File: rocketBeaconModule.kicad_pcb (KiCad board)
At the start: 2 copper layers, 80.5 x 49.3 mm, 72 parts, among them J1 TYPE-C-31-M-12, J2 Jumper Select, J3 Main Bus, P1 AntMount, U1 STM32F401CCU6, U2 AMS1117-3.3, U3 CC1200, X1 40mhz, Y1 16MHz

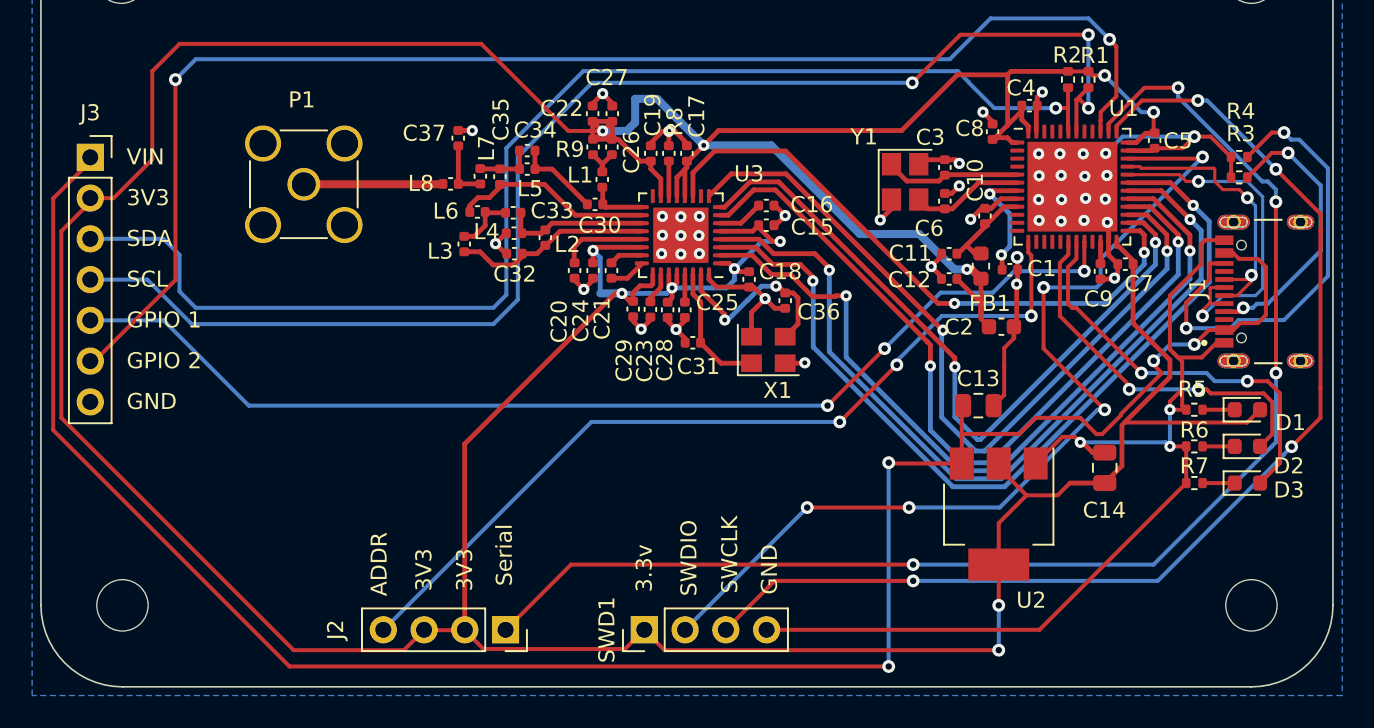
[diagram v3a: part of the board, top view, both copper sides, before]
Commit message: updated silk screen\nincreased spacing between leds\nchanged version number to 2.0
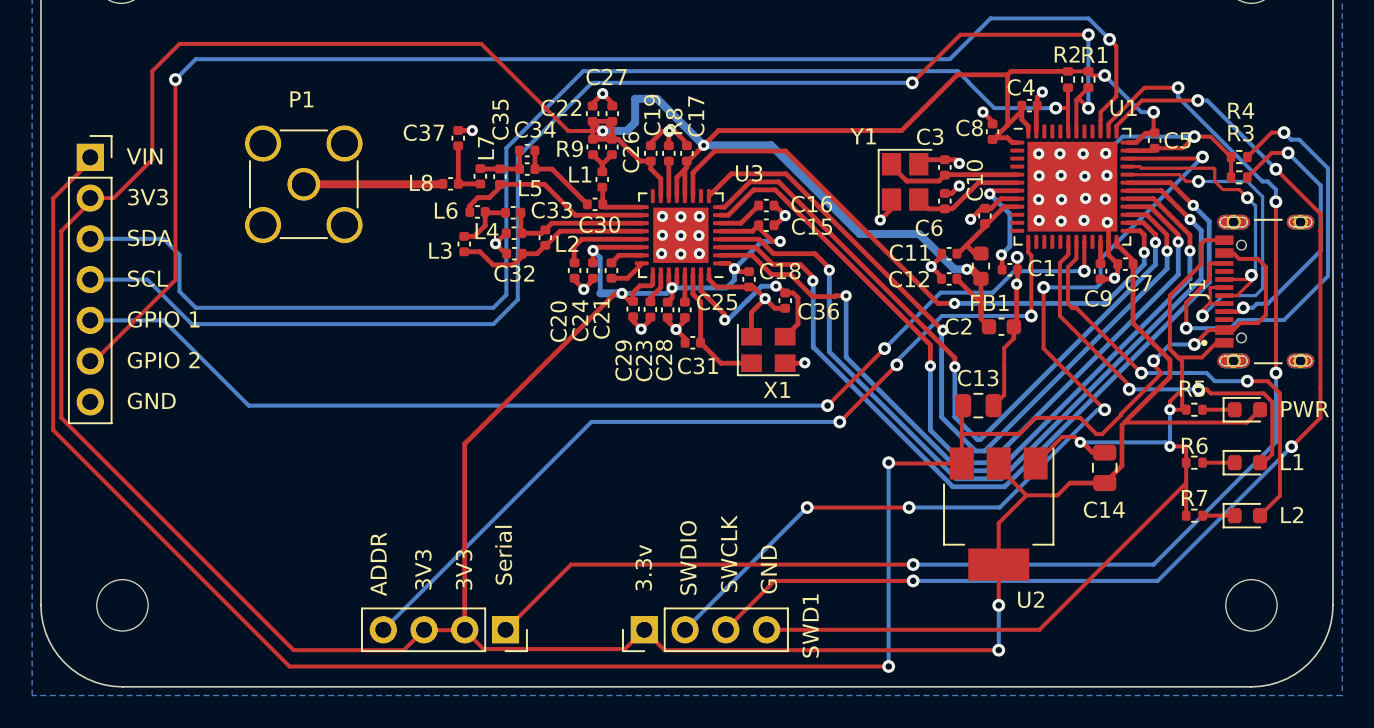
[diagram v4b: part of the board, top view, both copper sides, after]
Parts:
- J2: value Jumper Select -> MODE
- moved D3 2.03 mm to (225.0, 104.9)
- moved R7 2.03 mm to (221.7, 104.9)
- moved D2 1.02 mm to (225.0, 101.6)
- moved R6 1.02 mm to (221.7, 101.6)
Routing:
- net GND: track 136.8 -> 138.8 mm
- net /LED2: track 25.7 -> 27.7 mm
- net /LED1: track 23.5 -> 24.7 mm
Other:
- board text added: "L1"
- board text added: "L2"
- board text added: "PWR"
- board text added: "v2.0"
- board text removed: "v1.0"
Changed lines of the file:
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@@
   )
   (footprint "Resistor_SMD:R_0402_1005Metric" (layer "F.Cu")
-    (at 221.742 100.584 180)
+    (at 221.742 101.6 180)
     (descr "Resistor SMD 0402 (1005 Metric), square (rectangular) end terminal, IPC_7351 nominal, (Body size source: IPC-SM-782 page 72, https://www.pcb-3d.com/wordpress/wp-content/uploads/ipc-sm-782a_amendment_1_and_2.pdf), generated with kicad-footprint-generator")
     (tags "resistor")
@@
     (property "Sheetname" "")
     (attr smd)
-    (fp_text reference "D1" (at 2.688 0.808 180) (layer "F.SilkS")
+    (fp_text reference "D1" (at 2.688 0.808 180) (layer "F.SilkS") hide
       (effects (font (size 1 1) (thickness 0.15)))
     )
@@
   )
   (footprint "Resistor_SMD:R_0402_1005Metric" (layer "F.Cu")
-    (at 221.742 102.87 180)
+    (at 221.742 104.902 180)
     (descr "Resistor SMD 0402 (1005 Metric), square (rectangular) end terminal, IPC_7351 nominal, (Body size source: IPC-SM-782 page 72, https://www.pcb-3d.com/wordpress/wp-content/uploads/ipc-sm-782a_amendment_1_and_2.pdf), generated with kicad-footprint-generator")
     (tags "resistor")
@@
   )
   (footprint "LED_SMD:LED_0603_1608Metric" (layer "F.Cu")
-    (at 225.044 100.584)
+    (at 225.044 101.6)
     (descr "LED SMD 0603 (1608 Metric), square (rectangular) end terminal, IPC_7351 nominal, (Body size source: http://www.tortai-tech.com/upload/download/2011102023233369053.pdf), generated with kicad-footprint-generator")
     (tags "LED")
@@
     (property "Sheetname" "")
     (attr smd)
-    (fp_text reference "D2" (at 2.588 1.222) (layer "F.SilkS")
+    (fp_text reference "D2" (at 2.588 1.222) (layer "F.SilkS") hide
       (effects (font (size 1 1) (thickness 0.15)))
     )
-    (fp_text value "LED" (at 0 1.43) (layer "F.Fab")
+    (fp_text value "LED" (at 0 1.43) (layer "F.Fab") hide
       (effects (font (size 1 1) (thickness 0.15)))
     )
@@
     (property "Sheetname" "")
     (attr through_hole)
-    (fp_text reference "J2" (at 0 10.584 90) (layer "F.SilkS")
+    (fp_text reference "J2" (at 0 10.584 90) (layer "F.SilkS") hide
       (effects (font (size 1 1) (thickness 0.15)))
     )
-    (fp_text value "Jumper Select" (at 0 10.39 90) (layer "F.Fab")
+    (fp_text value "MODE" (at 0 10.39 90) (layer "F.Fab")
       (effects (font (size 1 1) (thickness 0.15)))
     )
@@
   )
   (footprint "LED_SMD:LED_0603_1608Metric" (layer "F.Cu")
-    (at 225.044 102.87)
+    (at 225.044 104.902)
     (descr "LED SMD 0603 (1608 Metric), square (rectangular) end terminal, IPC_7351 nominal, (Body size source: http://www.tortai-tech.com/upload/download/2011102023233369053.pdf), generated with kicad-footprint-generator")
     (tags "LED")
@@
     (property "Sheetname" "")
     (attr smd)
-    (fp_text reference "D3" (at 2.588 0.436) (layer "F.SilkS")
+    (fp_text reference "D3" (at 2.588 0.436) (layer "F.SilkS") hide
       (effects (font (size 1 1) (thickness 0.15)))
     )
-    (fp_text value "LED" (at 0 1.43) (layer "F.Fab")
+    (fp_text value "LED" (at 0 1.43) (layer "F.Fab") hide
       (effects (font (size 1 1) (thickness 0.15)))
     )
@@
     (property "Sheetname" "")
     (attr through_hole)
-    (fp_text reference "SWD1" (at 0 -2.33 90) (layer "F.SilkS")
+    (fp_text reference "SWD1" (at 0.254 10.404 90) (layer "F.SilkS")
       (effects (font (size 1 1) (thickness 0.15)))
     )
@@
     (property "Sheetname" "")
     (attr through_hole)
-    (fp_text reference "J3" (at 0 -2.77) (layer "F.SilkS")
+    (fp_text reference "J3" (at 0 -2.77) (layer "F.SilkS") hide
       (effects (font (size 1 1) (thickness 0.15)))
     )
@@
     (effects (font (size 2 2) (thickness 0.3)) (justify mirror))
   )
-  (gr_text "v1.0" (at 218.44 105.918) (layer "B.SilkS")
+  (gr_text "v2.0" (at 218.44 105.918) (layer "B.SilkS")
     (effects (font (size 1 1) (thickness 0.15)) (justify mirror))
   )
@@
     (effects (font (size 1 1) (thickness 0.15)) (justify right))
   )
+  (gr_text "L2" (at 227.838 104.902) (layer "F.SilkS")
+    (effects (font (size 1 1) (thickness 0.15)))
+  )
+  (gr_text "PWR" (at 228.6 98.298) (layer "F.SilkS")
+    (effects (font (size 1 1) (thickness 0.15)))
+  )
   (gr_text "GPIO 1" (at 155.194 92.71) (layer "F.SilkS")
     (effects (font (size 1 1) (thickness 0.15)) (justify left))
@@
     (effects (font (size 1 1) (thickness 0.15)) (justify left))
   )
+  (gr_text "L1" (at 227.838 101.6) (layer "F.SilkS")
+    (effects (font (size 1 1) (thickness 0.15)))
+  )
   (segment (start 209.76125 89.575) (end 209.76125 88.695) (width 0.3) (layer "F.Cu") (net 1))
   (segment (start 209.19075 84.65) (end 208.99125 84.8495) (width 0.3) (layer "F.Cu") (net 1))
@@
   (segment (start 216.154 100.97) (end 215.404 100.97) (width 0.3) (layer "F.Cu") (net 2))
   (segment (start 190.11625 81.845) (end 190.11625 81.7) (width 0.3) (layer "F.Cu") (net 2))
+  (segment (start 221.232 104.902) (end 221.232 102.87) (width 0.25) (layer "F.Cu") (net 2))
   (segment (start 195.61625 85.575) (end 196.24125 86.2) (width 0.3) (layer "F.Cu") (net 2))
   (segment (start 195.64125 86.8) (end 196.24125 86.2) (width 0.3) (layer "F.Cu") (net 2))
@@
   (segment (start 174.91125 84.225) (end 174.88625 84.25) (width 0.5) (layer "F.Cu") (net 32))
   (segment (start 174.88625 84.25) (end 166.24125 84.25) (width 0.5) (layer "F.Cu") (net 32))
-  (segment (start 222.252 100.584) (end 224.2565 100.584) (width 0.25) (layer "F.Cu") (net 35))
-  (segment (start 225.8315 100.584) (end 226.594 99.8215) (width 0.25) (layer "F.Cu") (net 36))
-  (segment (start 226.594 99.8215) (end 226.594 97.816521) (width 0.25) (layer "F.Cu") (net 36))
+  (segment (start 222.252 101.6) (end 224.2565 101.6) (width 0.25) (layer "F.Cu") (net 35))
+  (segment (start 226.594 101.066) (end 226.594 97.816521) (width 0.25) (layer "F.Cu") (net 36))
+  (segment (start 222.758 97.282) (end 222.504 97.028) (width 0.25) (layer "F.Cu") (net 36))
+  (segment (start 226.059478 97.282) (end 222.758 97.282) (width 0.25) (layer "F.Cu") (net 36))
   (segment (start 222.504 97.028) (end 221.996 97.028) (width 0.25) (layer "F.Cu") (net 36))
   (segment (start 213.89125 88.62275) (end 213.89125 87.8375) (width 0.25) (layer "F.Cu") (net 36))
-  (segment (start 226.594 97.816521) (end 226.059478 97.282) (width 0.25) (layer "F.Cu") (net 36))
   (segment (start 213.36 92.456) (end 213.36 89.154) (width 0.25) (layer "F.Cu") (net 36))
   (segment (start 213.36 89.154) (end 213.89125 88.62275) (width 0.25) (layer "F.Cu") (net 36))
-  (segment (start 222.758 97.282) (end 222.504 97.028) (width 0.25) (layer "F.Cu") (net 36))
+  (segment (start 225.8315 101.6) (end 226.06 101.6) (width 0.25) (layer "F.Cu") (net 36))
+  (segment (start 226.594 97.816521) (end 226.059478 97.282) (width 0.25) (layer "F.Cu") (net 36))
+  (segment (start 226.06 101.6) (end 226.594 101.066) (width 0.25) (layer "F.Cu") (net 36))
   (segment (start 217.678 96.774) (end 213.36 92.456) (width 0.25) (layer "F.Cu") (net 36))
-  (segment (start 226.059478 97.282) (end 222.758 97.282) (width 0.25) (layer "F.Cu") (net 36))
   (segment (start 217.678 97.028) (end 217.678 96.774) (width 0.25) (layer "F.Cu") (net 36))
   (via (at 217.678 97.028) (size 0.8) (drill 0.4) (layers "F.Cu" "B.Cu") (net 36))
@@
   (segment (start 229.616758 88.391242) (end 229.616758 84.328758) (width 0.25) (layer "B.Cu") (net 43))
   (segment (start 229.616758 84.328758) (end 227.584 82.296) (width 0.25) (layer "B.Cu") (net 43))
-  (segment (start 222.252 102.87) (end 224.2565 102.87) (width 0.25) (layer "F.Cu") (net 44))
-  (segment (start 227.076 97.282) (end 227.076 101.6255) (width 0.25) (layer "F.Cu") (net 45))
+  (segment (start 224.2565 104.902) (end 222.252 104.902) (width 0.25) (layer "F.Cu") (net 44))
+  (segment (start 227.076 103.6575) (end 225.8315 104.902) (width 0.25) (layer "F.Cu") (net 45))
   (segment (start 214.39125 91.96325) (end 218.44 96.012) (width 0.25) (layer "F.Cu") (net 45))
   (segment (start 213.868 91.694) (end 214.13725 91.96325) (width 0.25) (layer "F.Cu") (net 45))
   (segment (start 214.39125 88.88475) (end 213.868 89.408) (width 0.25) (layer "F.Cu") (net 45))
-  (segment (start 227.076 101.6255) (end 225.8315 102.87) (width 0.25) (layer "F.Cu") (net 45))
-  (segment (start 226.568 96.774) (end 227.076 97.282) (width 0.25) (layer "F.Cu") (net 45))
-  (segment (start 226.568 96.774) (end 226.314 96.52) (width 0.25) (layer "F.Cu") (net 45))
-  (segment (start 226.314 96.52) (end 225.044 96.52) (width 0.25) (layer "F.Cu") (net 45))
+  (segment (start 225.044 96.52) (end 226.314 96.52) (width 0.25) (layer "F.Cu") (net 45))
+  (segment (start 226.314 96.52) (end 227.076 97.282) (width 0.25) (layer "F.Cu") (net 45))
   (segment (start 214.13725 91.96325) (end 214.39125 91.96325) (width 0.25) (layer "F.Cu") (net 45))
   (segment (start 213.868 89.408) (end 213.868 91.694) (width 0.25) (layer "F.Cu") (net 45))
   (segment (start 214.39125 87.8375) (end 214.39125 88.88475) (width 0.25) (layer "F.Cu") (net 45))
+  (segment (start 227.076 97.282) (end 227.076 103.6575) (width 0.25) (layer "F.Cu") (net 45))
   (via (at 218.44 96.012) (size 0.8) (drill 0.4) (layers "F.Cu" "B.Cu") (net 45))
   (via (at 225.044 96.52) (size 0.8) (drill 0.4) (layers "F.Cu" "B.Cu") (net 45))

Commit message: Set Version 1.1
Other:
- board text added: "v1.1"
- board text removed: "v2.0"
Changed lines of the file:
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@@
     (effects (font (size 2 2) (thickness 0.3)) (justify mirror))
   )
-  (gr_text "v2.0" (at 218.44 105.918) (layer "B.SilkS")
+  (gr_text "v1.1" (at 218.44 105.918) (layer "B.SilkS")
     (effects (font (size 1 1) (thickness 0.15)) (justify mirror))
   )

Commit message: V3 changes
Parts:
- removed C14: 22u, Capacitor_SMD:C_0805_2012Metric
- removed J2: MODE, Connector_PinSocket_2.54mm:PinSocket_1x04_P2.54mm_Vertical
- removed J3: Main Bus, Connector_PinSocket_2.54mm:PinSocket_1x07_P2.54mm_Vertical
- removed R2: 1.5k, Resistor_SMD:R_0402_1005Metric
- added D4: TXT, LED_SMD:LED_0402_1005Metric, F.Cu at (93.7, 117.9)
- added D5: RXT, LED_SMD:LED_0402_1005Metric, F.Cu at (93.7, 118.9)
- added EX1: EXT1, Connector_FFC-FPC:Molex_200528-0080_1x08-1MP_P1.00mm_Horizontal, F.Cu at (72.0, 111.2)
- added R10: 1k, Resistor_SMD:R_0402_1005Metric, F.Cu at (93.7, 116.8)
- added R11: 1k, Resistor_SMD:R_0402_1005Metric, F.Cu at (93.7, 119.9)
- added R12: 5.11k, Resistor_SMD:R_0402_1005Metric, F.Cu at (84.2, 120.1)
- C1: value 100n -> 4.7uF; footprint Capacitor_SMD:C_0402_1005Metric -> Capacitor_SMD:C_0603_1608Metric
- C10: value 10n -> 10nF
- C11, C12: value 1u -> 1uF
- C13: value 22u -> 100nF; footprint Capacitor_SMD:C_0805_2012Metric -> Capacitor_SMD:C_0402_1005Metric
- C2: value 10u -> 10uF
- C3, C6: value 10p -> 10pF
- C4, C5, C7, C8: value 100n -> 100nF
- C9: value 2.2u -> 2.2uF
- D1: value LED -> PWR_LED; footprint LED_SMD:LED_0603_1608Metric -> LED_SMD:LED_0402_1005Metric
- D2, D3: footprint LED_SMD:LED_0603_1608Metric -> LED_SMD:LED_0402_1005Metric
- H1, H2, H3, H4: footprint MountingHole:MountingHole_3.2mm_M3 -> MountingHole:MountingHole_2.2mm_M2
- R1: value 1.5k -> 5.11k
- R9: value 18 -> 18k
- SWD1: footprint Connector_PinHeader_2.54mm:PinHeader_1x04_P2.54mm_Vertical -> Connector_PinSocket_1.27mm:PinSocket_1x05_P1.27mm_Vertical
- U2: value AMS1117-3.3 -> CP2102N-Axx-xQFN20; footprint Package_TO_SOT_SMD:SOT-223-3_TabPin2 -> CP2102:WFQFN-20
- X1: value 40mhz -> 40MHz
- moved H3 181.8 mm to (57.5, 141.2)
- moved D2 177.6 mm to (50.3, 133.3)
- moved D3 177.2 mm to (50.3, 134.4)
- moved R6 174.2 mm to (50.3, 132.3), turned to 0 degrees
- moved R7 174.1 mm to (50.3, 135.4), turned to 0 degrees
- moved C5 163.3 mm to (64.8, 134.5), turned to 0 degrees
- moved C7 160.6 mm to (63.3, 134.1), turned to 90 degrees
- moved FB1 159.0 mm to (59.6, 145.0)
- moved C9 156.8 mm to (68.9, 144.4)
- moved C6 156.8 mm to (58.5, 138.2), turned to 180 degrees
- moved U1 156.4 mm to (67.6, 139.3)
- moved C10 156.0 mm to (62.9, 141.8), turned to -90 degrees
- moved C3 155.8 mm to (58.5, 132.9), turned to 0 degrees
- moved C12 155.7 mm to (60.9, 145.4), turned to 90 degrees
- moved C4 154.9 mm to (70.7, 144.0), turned to 180 degrees
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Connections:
- net /PWR_LED_K renamed Net-(D1-Pad1)
- C1 pad 1: /NRST -> +3.3V
- C13 pad 1: VBUS -> +3.3V
- J1 pad A6: /USB_D+ -> /D+
- J1 pad A7: /USB_D- -> /D-
- J1 pad B6: /USB_D+ -> /D+
- J1 pad B7: /USB_D- -> /D-
- J1 pad S1: unconnected-(J1-PadS1) -> GND
- J1 pad S2: unconnected-(J1-PadS2) -> GND
- J1 pad S3: unconnected-(J1-PadS3) -> GND
- J1 pad S4: unconnected-(J1-PadS4) -> GND
- R1 pad 1: +3.3V -> /NRST
- R1 pad 2: /I2C_SCL -> +3.3V
- SWD1 pad 2: /SWDIO -> /SWCLK
- SWD1 pad 3: /SWCLK -> GND
- SWD1 pad 4: GND -> /SWDIO
- U1 pad 12: unconnected-(U1-Pad12) -> /CP2102N_SIG1
- U1 pad 13: /ADDR -> /CP2102N_SIG2
- U1 pad 16: unconnected-(U1-Pad16) -> RADIO_MARC_INT
- U1 pad 17: unconnected-(U1-Pad17) -> RADIO_INT
- U1 pad 18: /LED1 -> unconnected-(U1-Pad18)
- U1 pad 19: /LED2 -> unconnected-(U1-Pad19)
- U1 pad 20: /GPIO1 -> unconnected-(U1-Pad20)
- U1 pad 30: RADIO_INT -> /TX
- U1 pad 31: RADIO_MARC_INT -> /RX
- U1 pad 32: /USB_D- -> unconnected-(U1-Pad32)
- U1 pad 33: /USB_D+ -> unconnected-(U1-Pad33)
- U1 pad 38: /Serial -> unconnected-(U1-Pad38)
- U1 pad 39: /GPIO2 -> unconnected-(U1-Pad39)
- U1 pad 42: /I2C_SCL -> /LED2
- U1 pad 43: /I2C_SDA -> /LED1
- U1 pad 45: unconnected-(U1-Pad45) -> /S1
- U1 pad 46: unconnected-(U1-Pad46) -> /S2
- U2 pad 1: GND -> /CP2102N_SIG2
- U2 pad 2: +3.3V -> /CP2102N_SIG1
- U2 pad 3: VBUS -> GND
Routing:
- net +3.3V: track 323.7 -> 212.1 mm, vias 12 -> 13
- net VBUS: track 127.2 -> 35.1 mm, vias 4 -> 3
- net /GPIO2: track 86.2 -> 0.00 mm, vias 2 -> 0
- net /I2C_SCL: track 84.4 -> 0.00 mm, vias 3 -> 0
- net /Serial: track 83.4 -> 0.00 mm, vias 4 -> 0
- net /I2C_SDA: track 79.0 -> 0.00 mm, vias 1 -> 0
- net /CP2102N_SIG1: track 0.00 -> 70.0 mm, vias 0 -> 2
- net /CP2102N_SIG2: track 0.00 -> 69.4 mm, vias 0 -> 4
- net /GPIO1: track 69.2 -> 0.00 mm, vias 3 -> 0
- net /TX: track 0.00 -> 59.7 mm, vias 0 -> 3
- net /RX: track 0.00 -> 59.7 mm, vias 0 -> 3
- net /NRST: track 7.27 -> 63.3 mm
- net /ADDR: track 53.3 -> 0.00 mm, vias 3 -> 0
- net /SWCLK: track 71.9 -> 26.8 mm, vias 4 -> 2
- net /SWDIO: track 59.9 -> 25.9 mm, vias 5 -> 1
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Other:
- board size 80.5 x 49.3 mm -> 46.2 x 46.3 mm
- board text added: "50mm"
- board text added: "ArmstrongLabs"
- board text added: "Flash"
- board text added: "RX"
- board text added: "SubGhz Transciever"
- board text added: "TX"
- board text added: "V3"
- board text added: "X GND RX TX S2 S1 3V3 VIN"
- board text removed: "3.3v"
- board text removed: "3V3"
- board text removed: "ADDR"
- board text removed: "Armstrong Labs"
- board text removed: "CC1200 Radio Module"
- board text removed: "GND"
- board text removed: "GPIO 1"
- board text removed: "GPIO 2"
- board text removed: "L1"
- board text removed: "L2"
- board text removed: "SCL"
- board text removed: "SDA"
- board text removed: "SWCLK"
- board text removed: "SWDIO"
- board text removed: "Serial"
- board text removed: "VIN"
- board text removed: "v1.1"
